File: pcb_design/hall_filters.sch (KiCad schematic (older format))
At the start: 11 parts

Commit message: Components placement, 3D models, updated some footprints to nominal IPC type
Signed-off-by: Marcos Chaparro <mchaparro@paltatech.com>
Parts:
- removed C4, C5, C6, C7: 4n7, CRF1:SMD-0603_c, symbol C-RESCUE-BLDC_4
- removed R10, R7, R8, R9: 10k, CRF1:SMD-0603_r, symbol R-RESCUE-BLDC_4
- removed R11, R12, R13: 2k2, CRF1:SMD-0603_r, symbol R-RESCUE-BLDC_4
- added C4: 4.7nF, IPC7351-Nominal:CAPC1608X55, symbol C-0603
- added D13, D14, D3: BAT54S, smd-semi:SOT-23, symbol BAT54S
- added R10, R7, R8, R9: 10k, IPC7351-Nominal:RESC1608X50, symbol R-0603

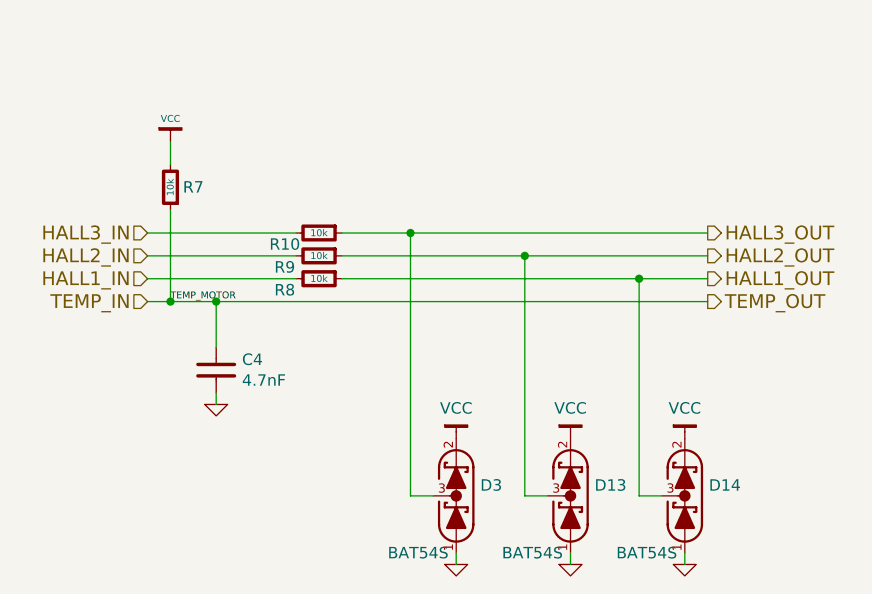
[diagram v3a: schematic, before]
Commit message: Added lp filters, fuses, tvs and power symbols
Signed-off-by: Marcos Chaparro <mchaparro@paltatech.com>
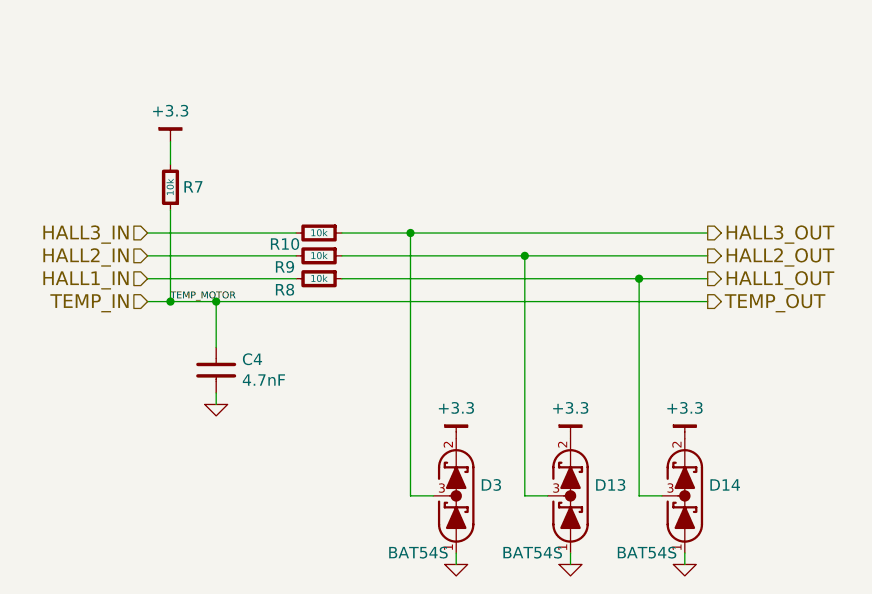
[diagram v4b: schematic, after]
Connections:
- net VCC renamed +3.3
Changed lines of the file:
@@
-	1    0    0    -1
-$EndComp
-$Comp
-L VCC #PWR25
-U 1 1 53FBB5DA
-P 4900 3150
-F 0 "#PWR25" H 4900 3250 30  0001 C CNN
-F 1 "VCC" H 4900 3250 30  0000 C CNN
-F 2 "" H 4900 3150 60  0001 C CNN
-F 3 "" H 4900 3150 60  0001 C CNN
-	1    4900 3150
 	1    0    0    -1
 $EndComp
@@
 $EndComp
 $Comp
-L VCC #PWR?
-U 1 1 588A8016
-P 6150 4450
-AR Path="/5886DA84/588A8016" Ref="#PWR?"  Part="1"
-AR Path="/588C2790/588A8016" Ref="#PWR?"  Part="1"
-AR Path="/588C4E84/588A8016" Ref="#PWR?"  Part="1"
-AR Path="/53FBA77E/588A8016" Ref="#PWR27"  Part="1"
-F 0 "#PWR27" H 6150 4500 30  0001 C CNN
-F 1 "VCC" H 6150 4583 50  0000 C CNN
-F 2 "" H 6150 4450 60  0000 C CNN
-F 3 "" H 6150 4450 60  0000 C CNN
-	1    6150 4450
-	1    0    0    -1
-$EndComp
-$Comp
 L GND-RESCUE-BLDC_4 #PWR28
 U 1 1 588A8030
@@
 $EndComp
 $Comp
-L VCC #PWR?
-U 1 1 588A842B
-P 6650 4450
-AR Path="/5886DA84/588A842B" Ref="#PWR?"  Part="1"
-AR Path="/588C2790/588A842B" Ref="#PWR?"  Part="1"
-AR Path="/588C4E84/588A842B" Ref="#PWR?"  Part="1"
-AR Path="/53FBA77E/588A842B" Ref="#PWR29"  Part="1"
-F 0 "#PWR29" H 6650 4500 30  0001 C CNN
-F 1 "VCC" H 6650 4583 50  0000 C CNN
-F 2 "" H 6650 4450 60  0000 C CNN
-F 3 "" H 6650 4450 60  0000 C CNN
-	1    6650 4450
-	1    0    0    -1
-$EndComp
-$Comp
 L GND-RESCUE-BLDC_4 #PWR30
 U 1 1 588A8431
@@
 $EndComp
 $Comp
-L VCC #PWR?
-U 1 1 588A87DC
-P 7150 4450
-AR Path="/5886DA84/588A87DC" Ref="#PWR?"  Part="1"
-AR Path="/588C2790/588A87DC" Ref="#PWR?"  Part="1"
-AR Path="/588C4E84/588A87DC" Ref="#PWR?"  Part="1"
-AR Path="/53FBA77E/588A87DC" Ref="#PWR31"  Part="1"
-F 0 "#PWR31" H 7150 4500 30  0001 C CNN
-F 1 "VCC" H 7150 4583 50  0000 C CNN
-F 2 "" H 7150 4450 60  0000 C CNN
-F 3 "" H 7150 4450 60  0000 C CNN
-	1    7150 4450
-	1    0    0    -1
-$EndComp
-$Comp
 L GND-RESCUE-BLDC_4 #PWR32
 U 1 1 588A87E2
@@
 Wire Wire Line
 	5100 4300 5100 4250
+$Comp
+L +3.3 #PWR?
+U 1 1 588B84F4
+P 4900 3150
+F 0 "#PWR?" H 0   100 30  0001 C CNN
+F 1 "+3.3" H 4900 3283 50  0000 C CNN
+F 2 "" H 0   50  60  0000 C CNN
+F 3 "" H 0   50  60  0000 C CNN
+	1    4900 3150
+	1    0    0    -1
+$EndComp
+$Comp
+L +3.3 #PWR?
+U 1 1 588B856B
+P 6150 4450
+F 0 "#PWR?" H 6200 4500 30  0001 C CNN
+F 1 "+3.3" H 6150 4583 50  0000 C CNN
+F 2 "" H -300 100 60  0000 C CNN
+F 3 "" H -300 100 60  0000 C CNN
+	1    6150 4450
+	1    0    0    -1
+$EndComp
+$Comp
+L +3.3 #PWR?
+U 1 1 588B8595
+P 6650 4450
+F 0 "#PWR?" H 6700 4500 30  0001 C CNN
+F 1 "+3.3" H 6650 4583 50  0000 C CNN
+F 2 "" H 200 100 60  0000 C CNN
+F 3 "" H 200 100 60  0000 C CNN
+	1    6650 4450
+	1    0    0    -1
+$EndComp
+$Comp
+L +3.3 #PWR?
+U 1 1 588B85B8
+P 7150 4450
+F 0 "#PWR?" H 7200 4500 30  0001 C CNN
+F 1 "+3.3" H 7150 4583 50  0000 C CNN
+F 2 "" H 700 100 60  0000 C CNN
+F 3 "" H 700 100 60  0000 C CNN
+	1    7150 4450
+	1    0    0    -1
+$EndComp
 $EndSCHEMATC
